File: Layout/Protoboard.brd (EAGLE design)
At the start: 100 x 80 mm, 3 parts

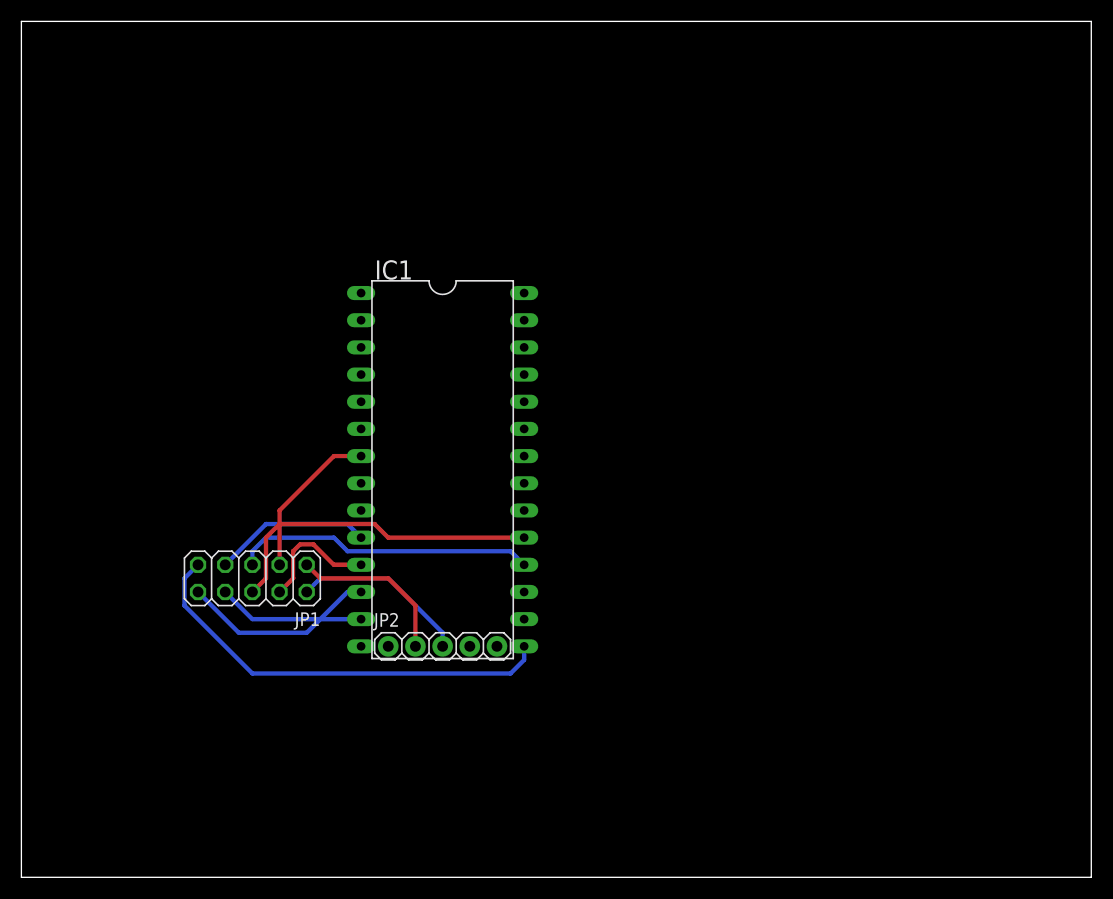
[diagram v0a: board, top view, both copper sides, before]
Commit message: add display enable/disable + images
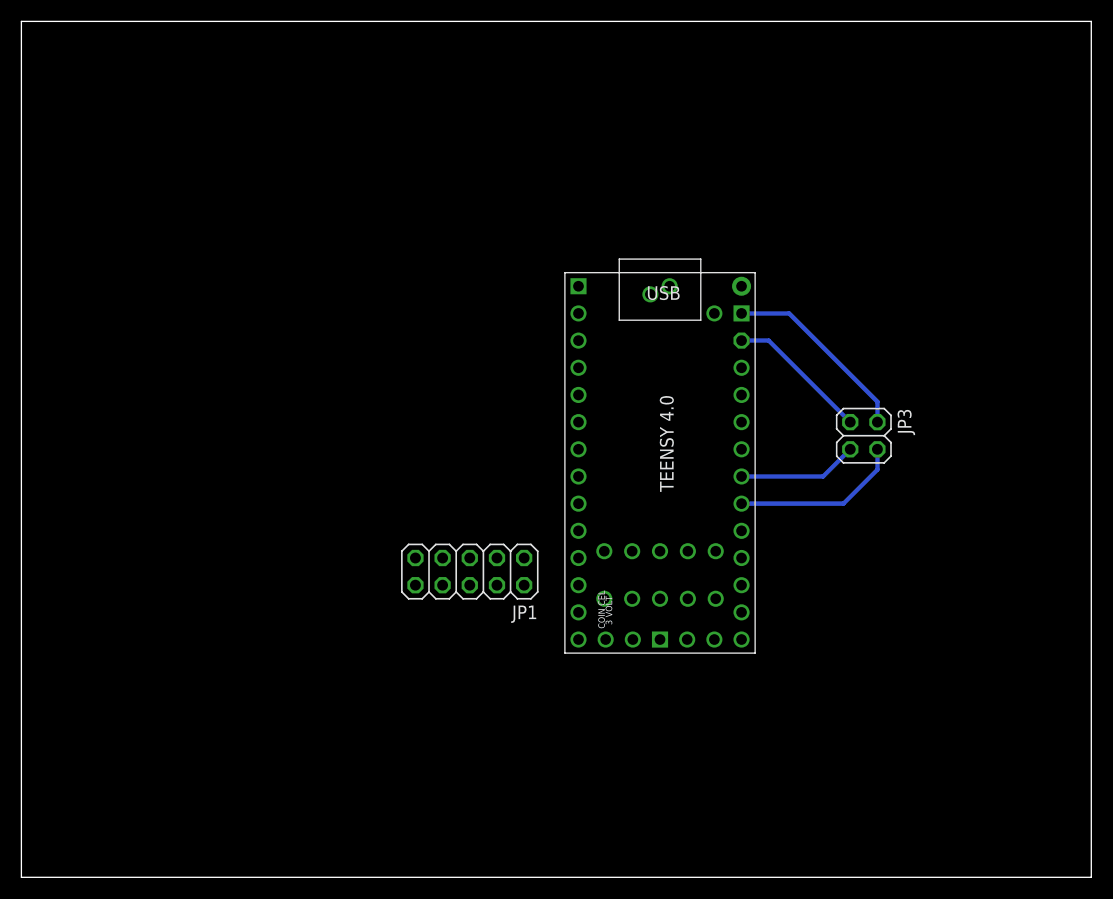
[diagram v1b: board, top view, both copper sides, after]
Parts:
- removed IC1: (no value), ic-package:DIL28-6
- removed JP2: (no value), pinhead:1X05
- added JP3: MLX, pinhead:2X02
- added U$1: TEENSY40, teensy:TEENSY40
- moved JP1 20.3 mm to (41.9, 28.6)
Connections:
- removed net N$9: IC1.7, JP1.3
- new net N$11: JP1.8, U$1.11-MOSI/CTX1
- new net N$12: JP1.10, U$1.10-CS/MQSR
- new net N$13: JP3.4, U$1.18-A4/SDA0
- new net N$14: JP3.3, U$1.19-A5/SCL0
- new net N$15: JP1.3, U$1.9-OUT1C
- net N$1: now also U$1.GND2; no longer JP2.3
- net N$10: now also U$1.5-IN2; no longer IC1.11
- net N$2: now also U$1.3V3-2; no longer JP2.2
- net N$3: now also JP3.1, U$1.3V3-1; no longer IC1.12, JP1.10
- net N$4: now also U$1.13-SCK/CRX1/LED; no longer IC1.15
- net N$5: now also JP3.2, U$1.GND3; no longer IC1.13, JP1.8
- net N$6: now also U$1.8-TX2/IN1; no longer IC1.10
- net N$7: now also U$1.16-A2/RX4/SCL1; no longer IC1.18
- net N$8: now also U$1.17-A3/TX4/SDA1; no longer IC1.19
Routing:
- net N$4: track 40.5 -> 0.00 mm
- net N$8: track 30.8 -> 0.00 mm
- net N$7: track 28.2 -> 0.00 mm
- net N$1: track 16.6 -> 0.00 mm
- net N$13: track 0.00 -> 15.9 mm
- net N$2: track 15.5 -> 0.00 mm
- net N$6: track 14.8 -> 0.00 mm
- net N$9: track 14.8 -> 0.00 mm
- net N$10: track 11.7 -> 0.00 mm
- net N$14: track 0.00 -> 11.2 mm
- net N$3: track 18.4 -> 13.3 mm
- net N$5: track 13.8 -> 18.0 mm
